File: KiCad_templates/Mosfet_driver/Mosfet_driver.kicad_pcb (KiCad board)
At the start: 2 copper layers, 75 x 40 mm, 62 parts, among them J1 KLS S1G03C, J2 KLS S1G03C, J3 KLS S1G03C, J4 KLS S1G02C, J5 KLS S1G02C, U1 MGJ2D051505SC, U2 MGJ2D051505SC, U3 UCC21520ADW, U4 74HC14

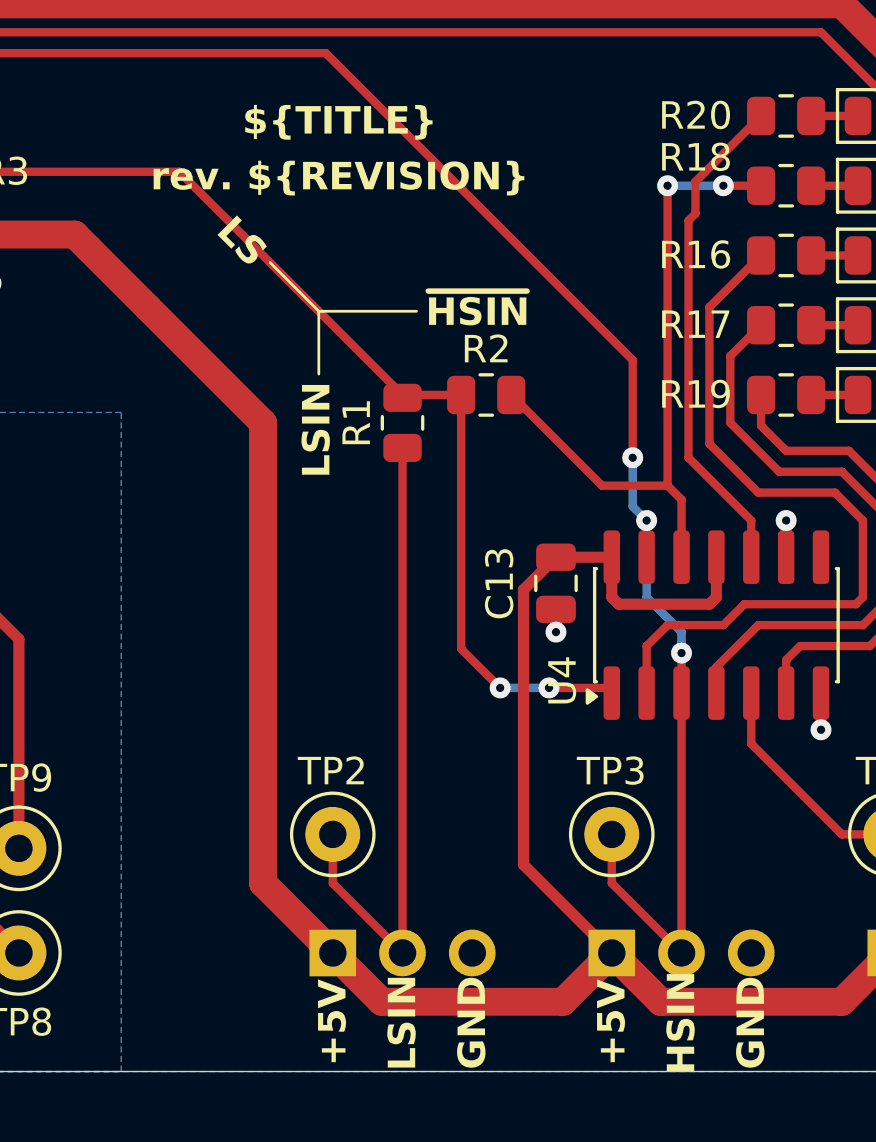
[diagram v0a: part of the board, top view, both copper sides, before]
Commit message: Doplnen text do schematu a na dps
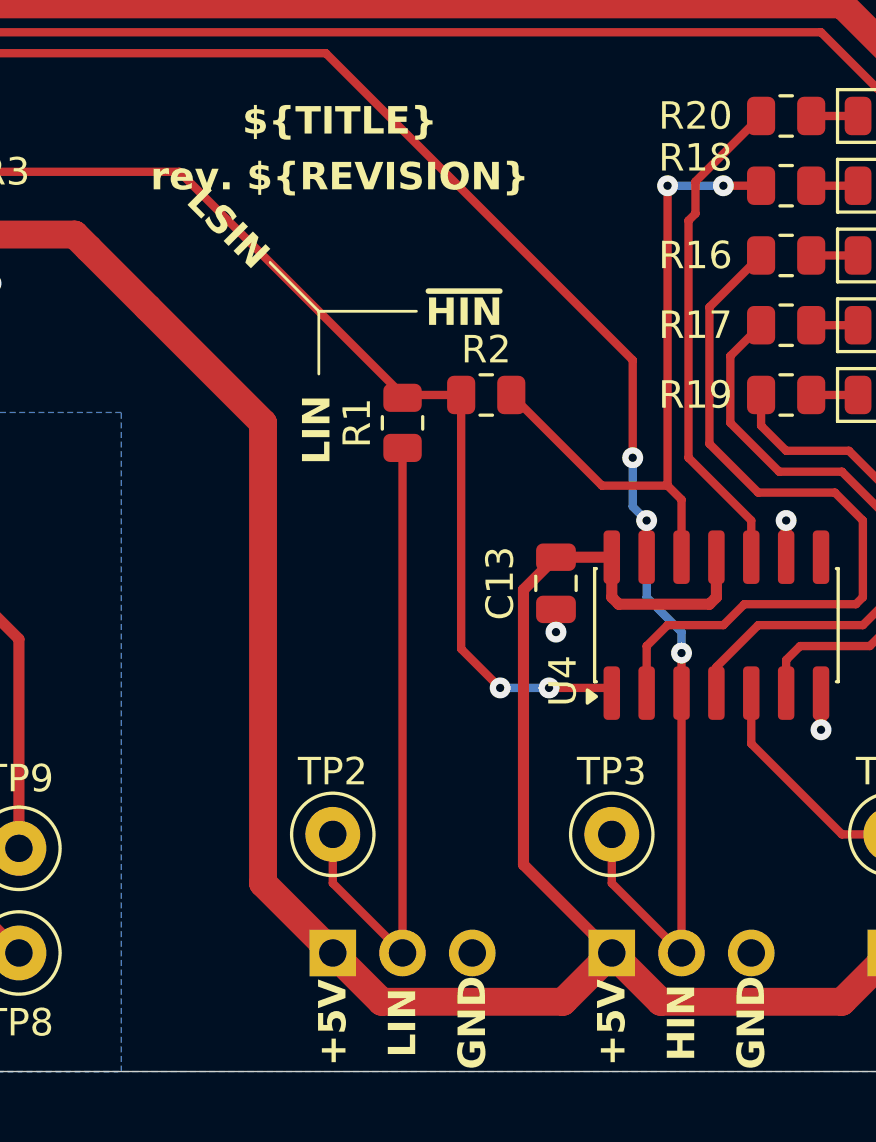
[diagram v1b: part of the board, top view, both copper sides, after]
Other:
- board text added: "HIN"
- board text added: "LIN"
- board text added: "~{HIN}"
- board text removed: "HSIN"
- board text removed: "~{HSIN}"
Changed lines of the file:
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@@
 		)
 	)
-	(gr_text "LS"
-		(at 144.526 94.488 315)
+	(gr_text "LSIN"
+		(at 144.018 93.98 315)
 		(layer "F.SilkS")
 		(effects
@@
 		)
 	)
-	(gr_text "~{HSIN}"
+	(gr_text "~{HIN}"
 		(at 151.207732 97.645731 0)
 		(layer "F.SilkS")
@@
 		)
 	)
-	(gr_text "LSIN"
+	(gr_text "LIN"
 		(at 147.828 101.346 90)
 		(layer "F.SilkS")
@@
 		)
 	)
-	(gr_text "LSIN"
+	(gr_text "LIN"
 		(at 150.368 122.936 90)
 		(layer "F.SilkS")
@@
 		)
 	)
-	(gr_text "HSIN"
+	(gr_text "HIN"
 		(at 160.528 122.936 90)
 		(layer "F.SilkS")
